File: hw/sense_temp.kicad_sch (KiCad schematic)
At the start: 3 parts

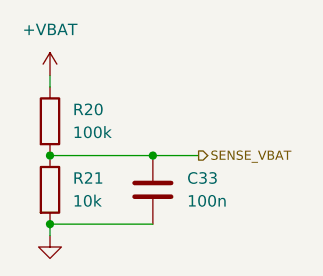
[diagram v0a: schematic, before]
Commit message: began with lcsc and footprints
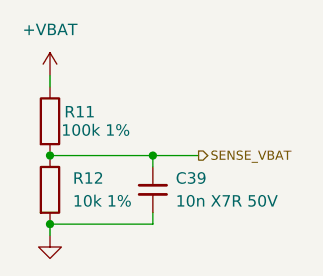
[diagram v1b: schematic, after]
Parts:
- removed C33: 100n, symbol Device:C
- removed R20: 100k, LED_SMD:LED_SK6805_PLCC4_2.4x2.7mm_P1.3mm, symbol Device:R
- removed R21: 10k, LED_SMD:LED_SK6805_PLCC4_2.4x2.7mm_P1.3mm, symbol Device:R
- added C39: 10n X7R 50V, Capacitor_SMD:C_0603_1608Metric, symbol Device:C_Small
- added R11: 100k 1%, Resistor_SMD:R_0603_1608Metric, symbol Device:R
- added R12: 10k 1%, Resistor_SMD:R_0603_1608Metric, symbol Device:R
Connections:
- net +VBAT: now also R11.1
- net GND: now also C39.2, R12.2
- net SENSE_VBAT: now also C39.1, R11.2, R12.1
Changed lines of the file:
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@@
 	(paper "A4")
+	(junction
+		(at 114.3 68.58)
+		(diameter 0)
+		(color 0 0 0 0)
+	)
+	(junction
+		(at 114.3 76.2)
+		(diameter 0)
+		(color 0 0 0 0)
+	)
 	(junction
 		(at 125.73 68.58)
@@
 		(color 0 0 0 0)
 	)
-	(junction
-		(at 114.3 68.58)
-		(diameter 0)
-		(color 0 0 0 0)
-	)
-	(junction
-		(at 114.3 76.2)
-		(diameter 0)
-		(color 0 0 0 0)
+	(wire
+		(pts
+			(xy 114.3 68.58) (xy 125.73 68.58)
+		)
+		(stroke
+			(width 0)
+			(type default)
+		)
+	)
+	(wire
+		(pts
+			(xy 114.3 76.2) (xy 125.73 76.2)
+		)
+		(stroke
+			(width 0)
+			(type default)
+		)
+	)
+	(wire
+		(pts
+			(xy 125.73 74.93) (xy 125.73 76.2)
+		)
+		(stroke
+			(width 0)
+			(type default)
+		)
 	)
 	(wire
@@
 	(wire
 		(pts
-			(xy 114.3 76.2) (xy 125.73 76.2)
+			(xy 125.73 68.58) (xy 125.73 69.85)
 		)
 		(stroke
@@
 		(pts
 			(xy 114.3 77.47) (xy 114.3 76.2)
-		)
-		(stroke
-			(width 0)
-			(type default)
-		)
-	)
-	(wire
-		(pts
-			(xy 114.3 68.58) (xy 125.73 68.58)
 		)
 		(stroke
@@
 	(symbol
 		(lib_id "Device:R")
-		(at 114.3 64.77 0)
+		(at 114.3 72.39 0)
 		(unit 1)
 		(body_style 1)
@@
 		(dnp no)
 		(fields_autoplaced yes)
-		(property "Reference" "R20"
-			(at 116.84 63.4999 0)
+		(property "Reference" "R12"
+			(at 116.84 71.12 0)
 			(show_name no)
 			(do_not_autoplace no)
@@
 			)
 		)
-		(property "Value" "100k"
-			(at 116.84 66.0399 0)
+		(property "Value" "10k 1%"
+			(at 116.84 73.66 0)
 			(show_name no)
 			(do_not_autoplace no)
@@
 			)
 		)
-		(property "Footprint" "LED_SMD:LED_SK6805_PLCC4_2.4x2.7mm_P1.3mm"
-			(at 112.522 64.77 90)
+		(property "Footprint" "Resistor_SMD:R_0603_1608Metric"
+			(at 112.522 72.39 90)
 			(hide yes)
 			(show_name no)
@@
 		)
 		(property "Datasheet" ""
-			(at 114.3 64.77 0)
+			(at 114.3 72.39 0)
 			(hide yes)
 			(show_name no)
@@
 		)
 		(property "Description" "Resistor"
-			(at 114.3 64.77 0)
-			(hide yes)
-			(show_name no)
-			(do_not_autoplace no)
-			(effects
-				(font
-					(size 1.27 1.27)
-				)
-			)
+			(at 114.3 72.39 0)
+			(hide yes)
+			(show_name no)
+			(do_not_autoplace no)
+			(effects
+				(font
+					(size 1.27 1.27)
+				)
+			)
+		)
+		(property "LCSC" "C25804"
+			(at 114.3 72.39 0)
+			(hide yes)
+			(show_name no)
+			(do_not_autoplace no)
+			(effects
+				(font
+					(size 1.016 1.016)
+				)
+			)
+		)
+		(pin "2"
 		)
 		(pin "1"
-		)
-		(pin "2"
 		)
 		(instances
 			(project "atlas-electronics"
 				(path "/915bc1ff-7be5-4368-a2db-c4889af73afd/8b207c98-7a97-4a14-bebf-ea2600be8946"
-					(reference "R20")
+					(reference "R12")
 					(unit 1)
 				)
@@
 		(dnp no)
 		(fields_autoplaced yes)
-		(property "Reference" "#PWR020"
+		(property "Reference" "#PWR036"
 			(at 114.3 63.5 0)
 			(hide yes)
@@
 			(project "atlas-electronics"
 				(path "/915bc1ff-7be5-4368-a2db-c4889af73afd/8b207c98-7a97-4a14-bebf-ea2600be8946"
-					(reference "#PWR020")
+					(reference "#PWR036")
 					(unit 1)
 				)
@@
 	)
 	(symbol
-		(lib_id "Device:R")
-		(at 114.3 72.39 0)
-		(unit 1)
-		(body_style 1)
-		(exclude_from_sim no)
-		(in_bom yes)
-		(on_board yes)
-		(in_pos_files yes)
-		(dnp no)
-		(fields_autoplaced yes)
-		(property "Reference" "R21"
-			(at 116.84 71.1199 0)
-			(show_name no)
-			(do_not_autoplace no)
-			(effects
-				(font
-					(size 1.27 1.27)
-				)
-				(justify left)
-			)
-		)
-		(property "Value" "10k"
-			(at 116.84 73.6599 0)
-			(show_name no)
-			(do_not_autoplace no)
-			(effects
-				(font
-					(size 1.27 1.27)
-				)
-				(justify left)
-			)
-		)
-		(property "Footprint" "LED_SMD:LED_SK6805_PLCC4_2.4x2.7mm_P1.3mm"
-			(at 112.522 72.39 90)
-			(hide yes)
-			(show_name no)
-			(do_not_autoplace no)
-			(effects
-				(font
-					(size 1.27 1.27)
-				)
-			)
-		)
-		(property "Datasheet" ""
-			(at 114.3 72.39 0)
-			(hide yes)
-			(show_name no)
-			(do_not_autoplace no)
-			(effects
-				(font
-					(size 1.27 1.27)
-				)
-			)
-		)
-		(property "Description" "Resistor"
-			(at 114.3 72.39 0)
-			(hide yes)
-			(show_name no)
-			(do_not_autoplace no)
-			(effects
-				(font
-					(size 1.27 1.27)
-				)
-			)
-		)
-		(pin "1"
-		)
-		(pin "2"
-		)
-		(instances
-			(project "atlas-electronics"
-				(path "/915bc1ff-7be5-4368-a2db-c4889af73afd/8b207c98-7a97-4a14-bebf-ea2600be8946"
-					(reference "R21")
-					(unit 1)
-				)
-			)
-		)
-	)
-	(symbol
-		(lib_id "Device:C")
+		(lib_id "Device:C_Small")
 		(at 125.73 72.39 0)
 		(unit 1)
@@
 		(dnp no)
 		(fields_autoplaced yes)
-		(property "Reference" "C33"
-			(at 129.54 71.1199 0)
+		(property "Reference" "C39"
+			(at 128.27 71.12 0)
 			(show_name no)
 			(do_not_autoplace no)
@@
 			)
 		)
-		(property "Value" "100n"
-			(at 129.54 73.6599 0)
+		(property "Value" "10n X7R 50V"
+			(at 128.27 73.66 0)
 			(show_name no)
 			(do_not_autoplace no)
@@
 			)
 		)
-		(property "Footprint" ""
-			(at 126.6952 76.2 0)
+		(property "Footprint" "Capacitor_SMD:C_0603_1608Metric"
+			(at 125.73 72.39 0)
 			(hide yes)
 			(show_name no)
@@
 			)
 		)
-		(property "Description" "Unpolarized capacitor"
+		(property "Description" "Unpolarized capacitor, small symbol"
+			(at 125.73 82.55 0)
+			(hide yes)
+			(show_name no)
+			(do_not_autoplace no)
+			(effects
+				(font
+					(size 1.27 1.27)
+				)
+			)
+		)
+		(property "LCSC" "C57112"
 			(at 125.73 72.39 0)
 			(hide yes)
@@
 			(effects
 				(font
-					(size 1.27 1.27)
-				)
-			)
+					(size 1.016 1.016)
+				)
+			)
+		)
+		(pin "2"
 		)
 		(pin "1"
-		)
-		(pin "2"
 		)
 		(instances
 			(project "atlas-electronics"
 				(path "/915bc1ff-7be5-4368-a2db-c4889af73afd/8b207c98-7a97-4a14-bebf-ea2600be8946"
-					(reference "C33")
+					(reference "C39")
+					(unit 1)
+				)
+			)
+		)
+	)
+	(symbol
+		(lib_id "Device:R")
+		(at 114.3 64.77 0)
+		(unit 1)
+		(body_style 1)
+		(exclude_from_sim no)
+		(in_bom yes)
+		(on_board yes)
+		(in_pos_files yes)
+		(dnp no)
+		(property "Reference" "R11"
+			(at 117.602 63.754 0)
+			(show_name no)
+			(do_not_autoplace no)
+			(effects
+				(font
+					(size 1.27 1.27)
+				)
+			)
+		)
+		(property "Value" "100k 1%"
+			(at 119.38 65.786 0)
+			(show_name no)
+			(do_not_autoplace no)
+			(effects
+				(font
+					(size 1.27 1.27)
+				)
+			)
+		)
+		(property "Footprint" "Resistor_SMD:R_0603_1608Metric"
+			(at 112.522 64.77 90)
+			(hide yes)
+			(show_name no)
+			(do_not_autoplace no)
+			(effects
+				(font
+					(size 1.27 1.27)
+				)
+			)
+		)
+		(property "Datasheet" ""
+			(at 114.3 64.77 0)
+			(hide yes)
+			(show_name no)
+			(do_not_autoplace no)
+			(effects
+				(font
+					(size 1.27 1.27)
+				)
+			)
+		)
+		(property "Description" "Resistor"
+			(at 114.3 64.77 0)
+			(hide yes)
+			(show_name no)
+			(do_not_autoplace no)
+			(effects
+				(font
+					(size 1.27 1.27)
+				)
+			)
+		)
+		(property "LCSC" "C25803"
+			(at 114.3 64.77 90)
+			(hide yes)
+			(show_name no)
+			(do_not_autoplace no)
+			(effects
+				(font
+					(size 1.016 1.016)
+				)
+			)
+		)
+		(pin "2"
+		)
+		(pin "1"
+		)
+		(instances
+			(project "atlas-electronics"
+				(path "/915bc1ff-7be5-4368-a2db-c4889af73afd/8b207c98-7a97-4a14-bebf-ea2600be8946"
+					(reference "R11")
 					(unit 1)
 				)
@@
 		(dnp no)
 		(fields_autoplaced yes)
-		(property "Reference" "#PWR054"
+		(property "Reference" "#PWR037"
 			(at 114.3 83.82 0)
 			(hide yes)
@@
 			(project "atlas-electronics"
 				(path "/915bc1ff-7be5-4368-a2db-c4889af73afd/8b207c98-7a97-4a14-bebf-ea2600be8946"
-					(reference "#PWR054")
+					(reference "#PWR037")
 					(unit 1)
 				)

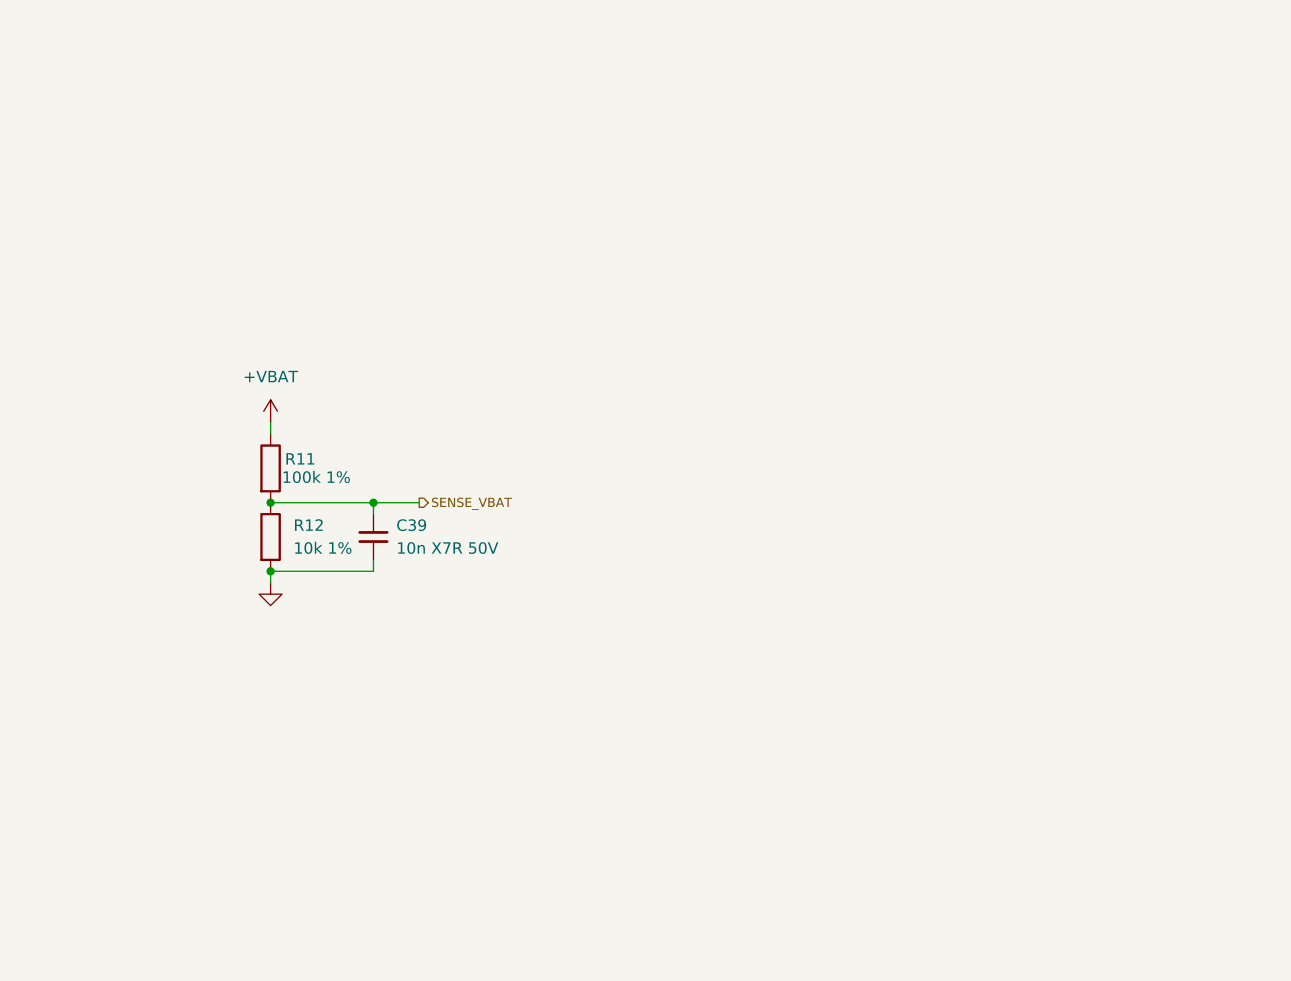
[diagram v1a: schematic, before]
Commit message: cleaned up *.kicad_sch
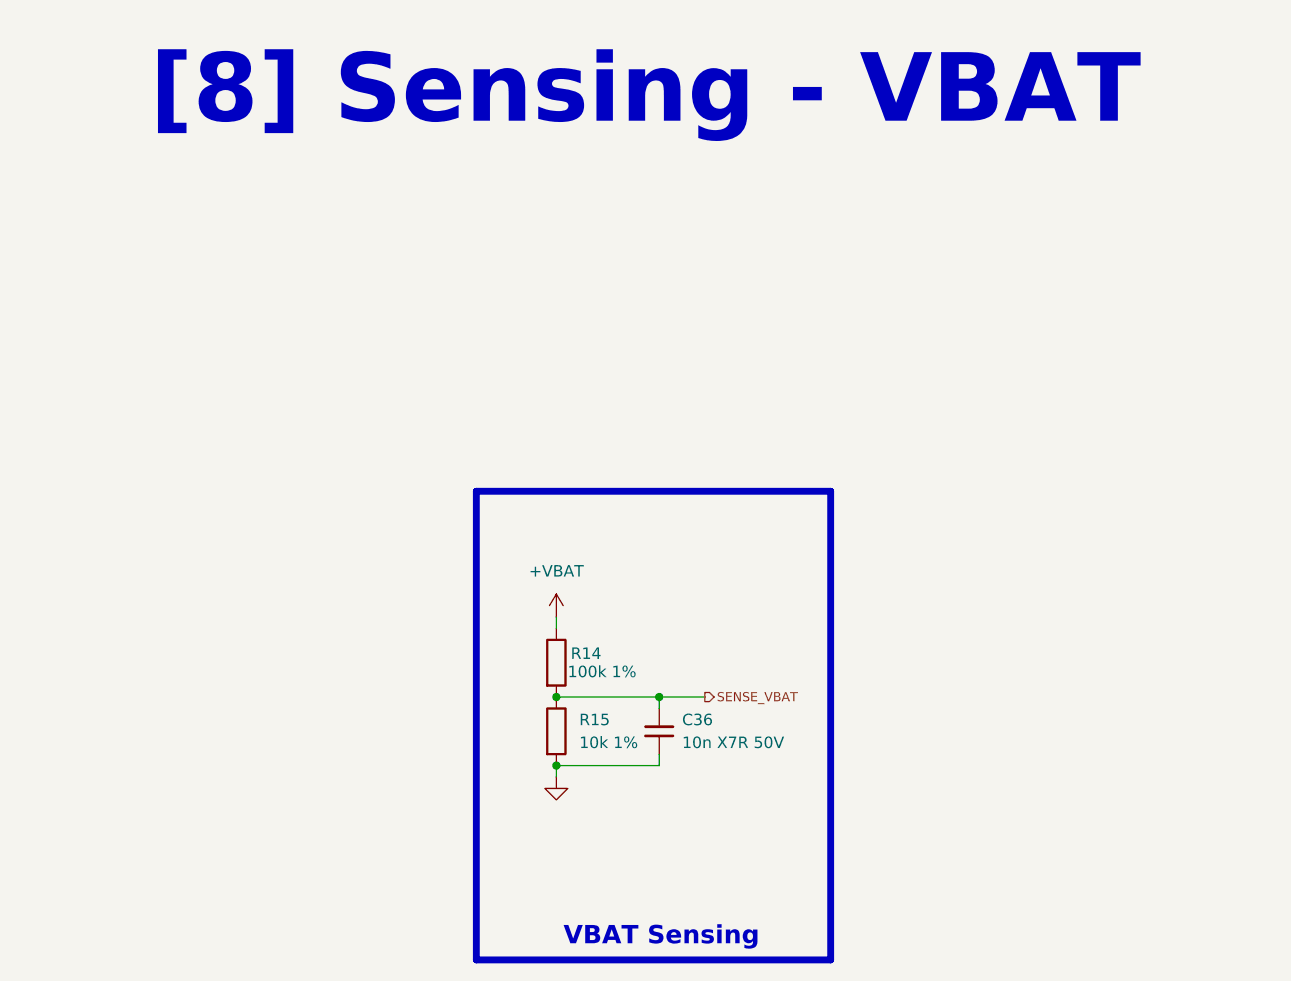
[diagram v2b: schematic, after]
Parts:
- renumbered C39 to C36, R11 to R14, R12 to R15
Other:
- note added: "VBAT Sensing"
- note added: "[8] Sensing - VBAT"
- moved on the sheet: C36, R14, R15

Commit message: extended lcsc number coverage
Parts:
- C36: VFD (none) -> Y
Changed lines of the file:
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@@
+			)
+		)
+		(property "VFD" ""
+			(at 146.05 93.98 0)
+			(hide yes)
+			(show_name no)
+			(do_not_autoplace no)
+			(effects
+				(font
+					(size 1.016 1.016)
+				)
 			)
 		)
@@
 			)
 		)
+		(property "VFD" "Y"
+			(at 157.48 93.98 0)
+			(hide yes)
+			(show_name no)
+			(do_not_autoplace no)
+			(effects
+				(font
+					(size 1.016 1.016)
+				)
+			)
+		)
 		(pin "2"
 		)
@@
 				)
 			)
+		)
+		(property "VFD" ""
+			(at 146.05 86.36 0)
+			(hide yes)
+			(show_name no)
+			(do_not_autoplace no)
+			(effects
+				(font
+					(size 1.016 1.016)
+				)
+			)

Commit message: extended lcsc number coverage and added status led
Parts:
- R14: VFD (none) -> Y
- R15: footprint Resistor_SMD:R_0603_1608Metric -> Resistor_SMD:R_0402_1005Metric; LCSC C25804 -> C25744; VFD (none) -> Y
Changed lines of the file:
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@@
 			)
 		)
-		(property "Footprint" "Resistor_SMD:R_0603_1608Metric"
+		(property "Footprint" "Resistor_SMD:R_0402_1005Metric"
 			(at 144.272 93.98 90)
 			(hide yes)
@@
 			)
 		)
-		(property "LCSC" "C25804"
+		(property "LCSC" "C25744"
 			(at 146.05 93.98 0)
 			(hide yes)
@@
 			)
 		)
-		(property "VFD" ""
+		(property "VFD" "Y"
 			(at 146.05 93.98 0)
 			(hide yes)
@@
 			)
 		)
-		(property "VFD" ""
+		(property "VFD" "Y"
 			(at 146.05 86.36 0)
 			(hide yes)
